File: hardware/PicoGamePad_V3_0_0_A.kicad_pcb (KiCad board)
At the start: 4 copper layers, 68.9 x 37.6 mm, 55 parts, among them J1 C116159, J3 RBP_GPIO_CONN, SW1 SW_Push, SW2 SW_Push, SW3 SW_Push, SW4 SW_Push, SW5 SW_Push, SW6 SW_Push, SW7 SW_Push, SW8 SW_Push, U1 ASM1117-3.3, U3 WQ25JVS, U4 RP2040, Y1 X322512MMB4SI

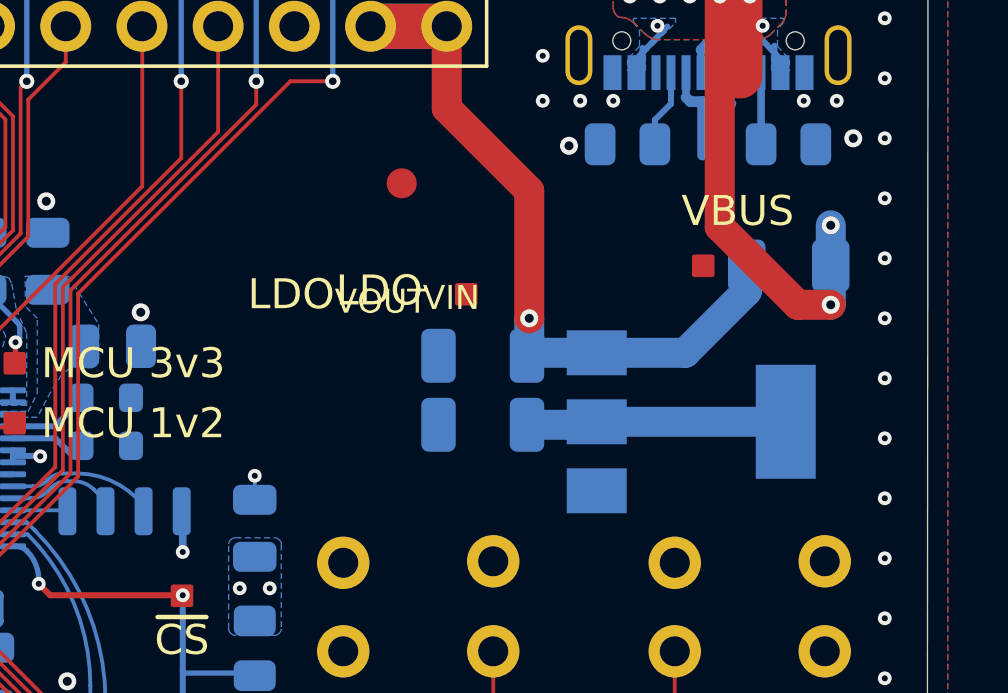
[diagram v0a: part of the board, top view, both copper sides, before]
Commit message: 
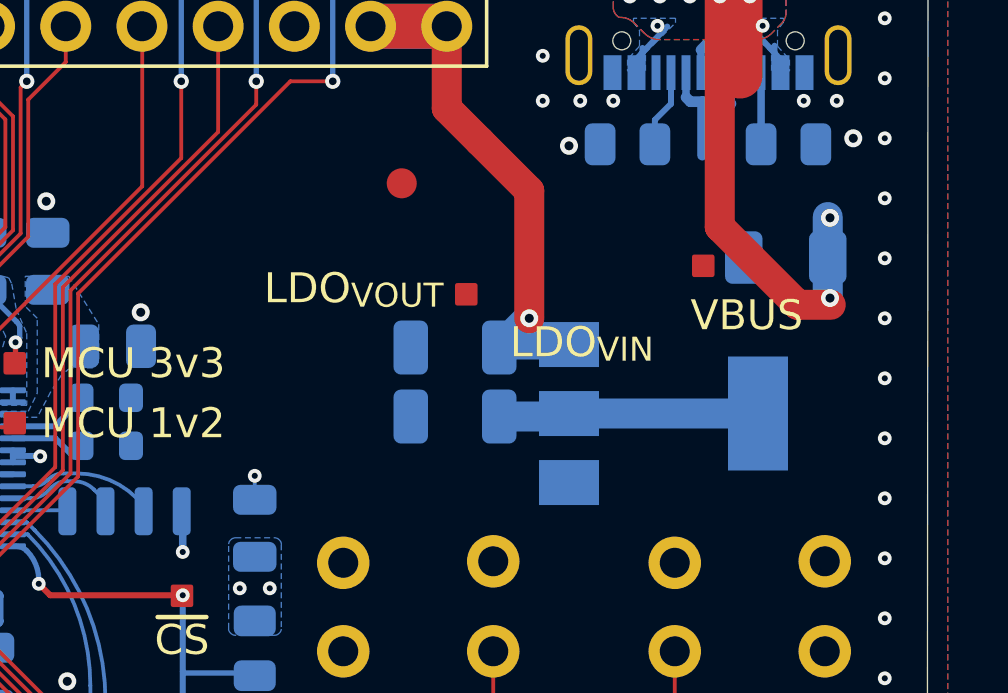
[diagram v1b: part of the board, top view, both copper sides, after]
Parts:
- moved U1 0.97 mm to (150.1, 73.2)
- moved C2 0.97 mm to (143.2, 71.0)
- moved C3 0.97 mm to (143.2, 73.3)
- moved F1 0.29 mm to (154.2, 68.0)
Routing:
- net VBUS: track 30.5 -> 23.9 mm
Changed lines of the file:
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@@
   (title_block
     (title "RP2040-Gamepad")
-    (date "2022-09-08")
-    (rev "4.0.0 (Rev A)")
-    (company "Michael Lloyd, UNSW Makerspaces")
+    (date "2023-02-24")
+    (rev "3.4.0 (Rev A)")
+    (company "UNSW Makerspaces")
   )
   (layers
@@
     (aux_axis_origin 125 75)
     (pcbplotparams
-      (layerselection 0x003d2f4_7ffffff8)
+      (layerselection 0x0001004_7ffffff8)
       (disableapertmacros false)
       (usegerberextensions false)
@@
       (svguseinch false)
       (svgprecision 6)
-      (excludeedgelayer true)
+      (excludeedgelayer false)
       (plotframeref false)
       (viasonmask false)
@@
       (hpglpendiameter 15.000000)
       (dxfpolygonmode true)
-      (dxfimperialunits true)
+      (dxfimperialunits false)
       (dxfusepcbnewfont true)
       (psnegative false)
@@
       (drillshape 0)
       (scaleselection 1)
-      (outputdirectory "fab/stencil/")
+      (outputdirectory "fab/board/")
     )
   )
@@
       (effects (font (size 1 1) (thickness 0.15)) (justify left))
     )
-    (fp_text value "LDO_{VIN}" (at -4.05 0.075 unlocked) (layer "F.SilkS")
+    (fp_text value "LDO_{VIN}" (at 1.75 1.8 unlocked) (layer "F.SilkS")
       (effects (font (size 1 1) (thickness 0.15)))
     )
@@
       (effects (font (size 1 1) (thickness 0.15)) (justify left))
     )
-    (fp_text value "LDO_{VOUT}" (at -4.291667 0 unlocked) (layer "F.SilkS")
+    (fp_text value "LDO_{VOUT}" (at -3.75 -0.2 unlocked) (layer "F.SilkS")
       (effects (font (size 1 1) (thickness 0.15)))
     )
@@
       (effects (font (size 1 1) (thickness 0.15)) (justify left))
     )
-    (fp_text value "VBUS" (at 1.15 -1.825 unlocked) (layer "F.SilkS")
+    (fp_text value "VBUS" (at 1.45 1.65 unlocked) (layer "F.SilkS")
       (effects (font (size 1 1) (thickness 0.15)))
     )
@@
   )
   (footprint "Package_TO_SOT_SMD:SOT-223-3_TabPin2" (layer "B.Cu")
-    (at 151.05 73.45)
+    (at 150.125 73.175)
     (descr "module CMS SOT223 4 pins")
     (tags "CMS SOT")
@@
   )
   (footprint "Capacitor_SMD:C_1206_3216Metric" (layer "B.Cu")
-    (at 144.1 73.55 180)
+    (at 143.175 73.275 180)
     (descr "Capacitor SMD 1206 (3216 Metric), square (rectangular) end terminal, IPC_7351 nominal, (Body size source: IPC-SM-782 page 76, https://www.pcb-3d.com/wordpress/wp-content/uploads/ipc-sm-782a_amendment_1_and_2.pdf), generated with kicad-footprint-generator")
     (tags "capacitor")
@@
   )
   (footprint "Capacitor_SMD:C_1206_3216Metric" (layer "B.Cu")
-    (at 144.1 71.25 180)
+    (at 143.175 70.975 180)
     (descr "Capacitor SMD 1206 (3216 Metric), square (rectangular) end terminal, IPC_7351 nominal, (Body size source: IPC-SM-782 page 76, https://www.pcb-3d.com/wordpress/wp-content/uploads/ipc-sm-782a_amendment_1_and_2.pdf), generated with kicad-footprint-generator")
     (tags "capacitor")
@@
   )
   (footprint "Fuse:Fuse_1206_3216Metric" (layer "B.Cu")
-    (at 154.3 68.25 180)
+    (at 154.2 67.975 180)
     (descr "Fuse SMD 1206 (3216 Metric), square (rectangular) end terminal, IPC_7351 nominal, (Body size source: http://www.tortai-tech.com/upload/download/2011102023233369053.pdf), generated with kicad-footprint-generator")
     (tags "fuse")
@@
   (segment (start 121.2 69.05) (end 121.227211 69.022789) (width 0.381) (layer "B.Cu") (net 1))
   (segment (start 119.057598 70.092402) (end 120.1 69.05) (width 0.3556) (layer "B.Cu") (net 1))
-  (segment (start 147.9 73.45) (end 154.2 73.45) (width 1) (layer "B.Cu") (net 1))
+  (segment (start 146.975 73.175) (end 153.275 73.175) (width 1) (layer "B.Cu") (net 1))
   (segment (start 127.75 79.05) (end 127.6 78.9) (width 0.1778) (layer "B.Cu") (net 1))
-  (segment (start 145.575 73.55) (end 147.8 73.55) (width 1) (layer "B.Cu") (net 1))
+  (segment (start 144.65 73.275) (end 146.875 73.275) (width 1) (layer "B.Cu") (net 1))
   (segment (start 125.322484 80.979685) (end 125.320087 80.982082) (width 0.3556) (layer "B.Cu") (net 1))
   (segment (start 128.437502 74.8) (end 128.437502 74.587502) (width 0.2) (layer "B.Cu") (net 1))
   (segment (start 123.993487 80.156513) (end 123.340188 80.809812) (width 0.3556) (layer "B.Cu") (net 1))
-  (segment (start 147.8 73.55) (end 147.9 73.45) (width 1) (layer "B.Cu") (net 1))
+  (segment (start 146.875 73.275) (end 146.975 73.175) (width 1) (layer "B.Cu") (net 1))
   (segment (start 121.360289 80.982082) (end 125.320087 80.982082) (width 0.3556) (layer "B.Cu") (net 1))
   (segment (start 121.360289 80.982082) (end 127.754217 80.982082) (width 0.508) (layer "B.Cu") (net 1))
@@
   (via (at 152.1 88.4) (size 0.6) (drill 0.3) (layers "F.Cu" "B.Cu") (net 2))
   (segment (start 142.9 60.265) (end 140.385 60.265) (width 1.5) (layer "B.Cu") (net 2))
-  (segment (start 145.65 70) (end 145.65 71.175) (width 1) (layer "B.Cu") (net 2))
-  (segment (start 150.85 71.15) (end 147.9 71.15) (width 1) (layer "B.Cu") (net 2))
-  (segment (start 145.65 71.175) (end 145.575 71.25) (width 1) (layer "B.Cu") (net 2))
+  (segment (start 145.65 70) (end 145.625 70) (width 1) (layer "B.Cu") (net 2))
   (segment (start 150.375 88.425) (end 150.4 88.4) (width 0.508) (layer "B.Cu") (net 2))
-  (segment (start 152.9 68.25) (end 152.9 69.1) (width 1) (layer "B.Cu") (net 2))
   (segment (start 150.4 88.4) (end 152.1 88.4) (width 0.508) (layer "B.Cu") (net 2))
+  (segment (start 145.625 70) (end 144.65 70.975) (width 1) (layer "B.Cu") (net 2))
   (segment (start 147.99 88.4) (end 150.35 88.4) (width 1) (layer "B.Cu") (net 2))
-  (segment (start 147.9 71.15) (end 145.675 71.15) (width 1) (layer "B.Cu") (net 2))
+  (segment (start 146.975 70.875) (end 144.75 70.875) (width 1) (layer "B.Cu") (net 2))
   (segment (start 150.35 88.4) (end 150.375 88.425) (width 0.508) (layer "B.Cu") (net 2))
   (segment (start 140.385 60.265) (end 140.35 60.3) (width 1) (layer "B.Cu") (net 2))
-  (segment (start 152.9 69.1) (end 150.85 71.15) (width 1) (layer "B.Cu") (net 2))
-  (segment (start 145.675 71.15) (end 145.575 71.25) (width 1) (layer "B.Cu") (net 2))
+  (segment (start 144.75 70.875) (end 144.65 70.975) (width 1) (layer "B.Cu") (net 2))
   (segment (start 149.8375 63.3875) (end 149.8375 64.2) (width 0.2) (layer "B.Cu") (net 3))
   (segment (start 150.375 62.85) (end 149.8375 63.3875) (width 0.2) (layer "B.Cu") (net 3))
@@
   (via (at 151 59.25) (size 0.508) (drill 0.254) (layers "F.Cu" "B.Cu") (free) (net 17))
   (via (at 152 58.25) (size 0.508) (drill 0.254) (layers "F.Cu" "B.Cu") (free) (net 17))
-  (via (at 155.7 66.9) (size 0.6) (drill 0.3) (layers "F.Cu" "B.Cu") (net 17))
+  (via (at 155.675 66.65) (size 0.6) (drill 0.3) (layers "F.Cu" "B.Cu") (net 17))
   (via (at 153 59.25) (size 0.508) (drill 0.254) (layers "F.Cu" "B.Cu") (free) (net 17))
   (via (at 150 59.25) (size 0.508) (drill 0.254) (layers "F.Cu" "B.Cu") (free) (net 17))
   (via (at 152 59.25) (size 0.508) (drill 0.254) (layers "F.Cu" "B.Cu") (free) (net 17))
   (via (at 149.925 60.25) (size 0.46) (drill 0.2) (layers "F.Cu" "B.Cu") (free) (net 17))
-  (via (at 155.7 69.55) (size 0.6) (drill 0.3) (layers "F.Cu" "B.Cu") (net 17))
+  (via (at 155.675 69.325) (size 0.6) (drill 0.3) (layers "F.Cu" "B.Cu") (net 17))
   (via (at 149 58.25) (size 0.508) (drill 0.254) (layers "F.Cu" "B.Cu") (free) (net 17))
   (via (at 149 59.25) (size 0.508) (drill 0.254) (layers "F.Cu" "B.Cu") (free) (net 17))
   (via (at 150 58.25) (size 0.508) (drill 0.254) (layers "F.Cu" "B.Cu") (free) (net 17))
-  (segment (start 155.7 68.25) (end 155.7 66.9) (width 1) (layer "B.Cu") (net 17))
+  (segment (start 155.6 67.975) (end 155.6 66.625) (width 1) (layer "B.Cu") (net 17))
   (segment (start 149.25 61.325) (end 150.25 60.275) (width 0.2) (layer "B.Cu") (net 17))
-  (segment (start 155.7 68.25) (end 155.7 69.55) (width 1) (layer "B.Cu") (net 17))
+  (segment (start 155.6 67.975) (end 155.6 69.275) (width 1) (layer "B.Cu") (net 17))
   (segment (start 154.1 61.45) (end 153.05 60.325) (width 0.2) (layer "B.Cu") (net 17))
   (segment (start 153.825 61.5375) (end 153.825 60.9125) (width 0.2) (layer "B.Cu") (net 17))
